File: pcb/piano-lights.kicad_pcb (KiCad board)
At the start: 2 copper layers, 98 x 51.6 mm, 40 parts, among them J1 USB-C 6-Pin, J2 FTDI RS232, J3 LED Strip, J4 AVR-ISP-6, J5 MIDI IN, J6 MIDI THRU, J7 MIDI Coupler B, J8 MIDI Coupler A, SW1 Button, SW2 Reset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

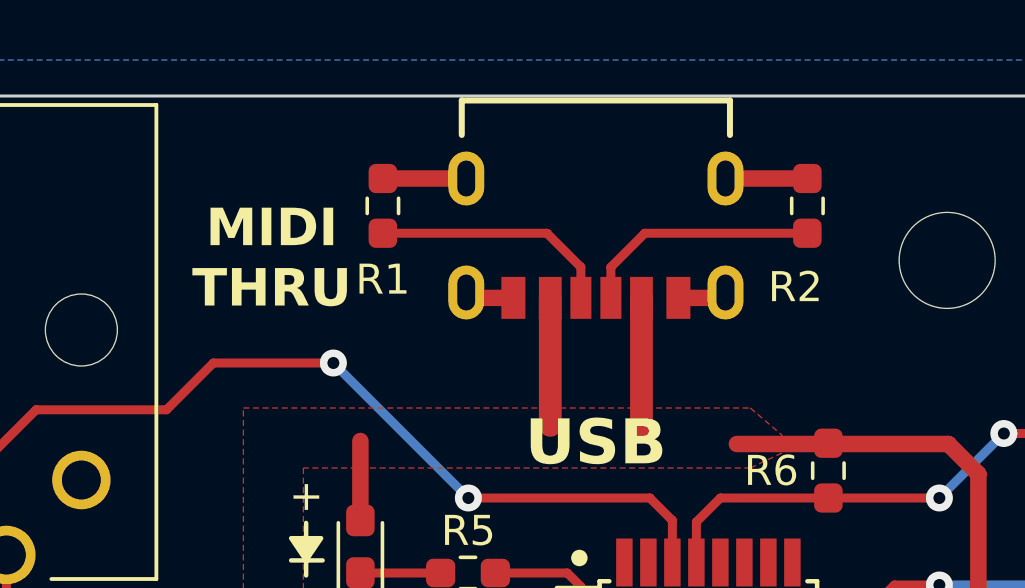
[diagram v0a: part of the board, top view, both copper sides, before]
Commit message: Tie USB-C shield to earth and add a 4n7F cap between earth and ground
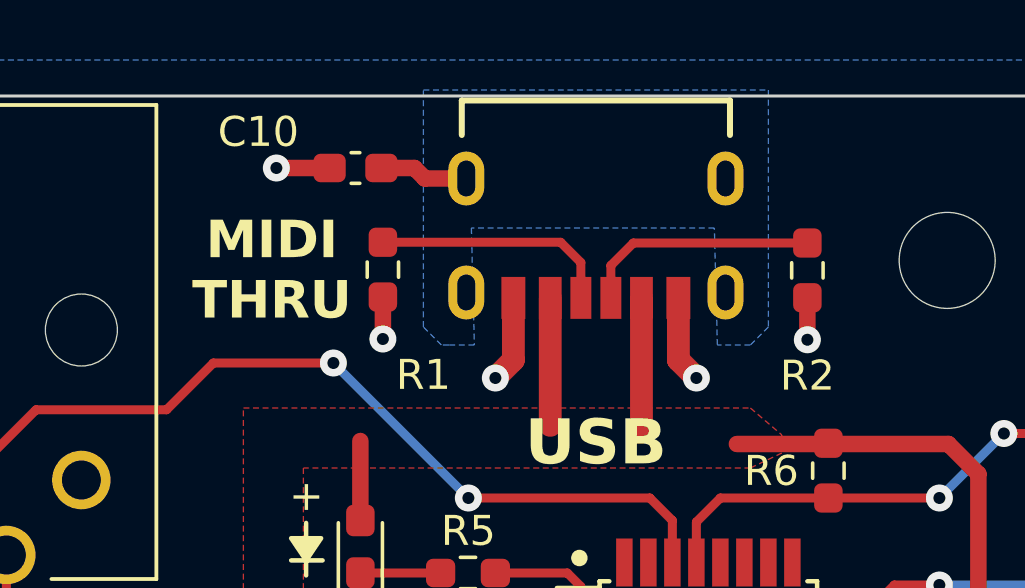
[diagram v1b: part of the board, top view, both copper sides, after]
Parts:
- added C10: 4n7, Capacitor_SMD:C_0603_1608Metric_Pad1.08x0.95mm_HandSolder, F.Cu at (149.8, 80.6)
- moved R2 2.15 mm to (164.9, 84.0), turned to -90 degrees
- moved R1 2.12 mm to (150.8, 84.0), turned to -90 degrees
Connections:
- J1 pad S1: GND -> Earth
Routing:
- net Earth: track 0.00 -> 2.97 mm
- net GND: track 32.7 -> 34.3 mm, vias 13 -> 18
- added copper zone on B.Cu, net Earth

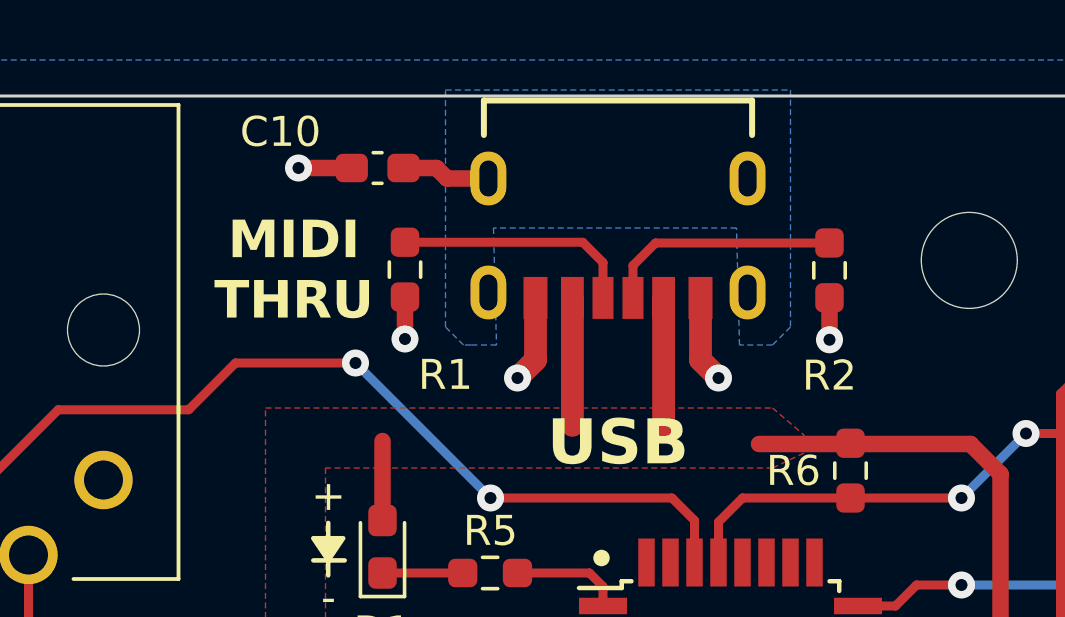
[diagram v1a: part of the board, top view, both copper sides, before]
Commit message: Reroute CC1 and CC2 to not cross ground split planes. Move Earth to front ground pour.
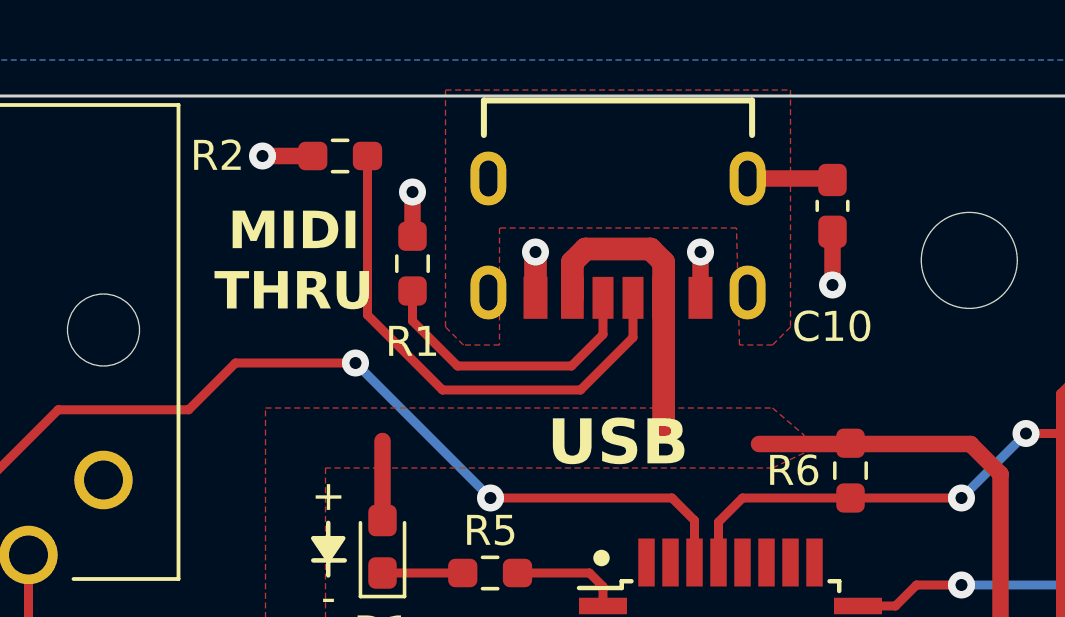
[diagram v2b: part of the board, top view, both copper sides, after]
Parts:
- moved R2 16.8 mm to (148.6, 80.2), turned to 180 degrees
- moved C10 15.2 mm to (165.0, 81.9), turned to 90 degrees
- moved R1 0.32 mm to (151.0, 83.8), turned to 90 degrees
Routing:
- net /USB_CC1: track 7.47 -> 17.2 mm
- net GND: track 34.3 -> 31.9 mm
- net /USB_CC2: track 7.71 -> 9.63 mm
- net +5V: track 130.0 -> 131.5 mm
- added copper zone on F.Cu, net Earth
- removed copper zone on B.Cu, net Earth

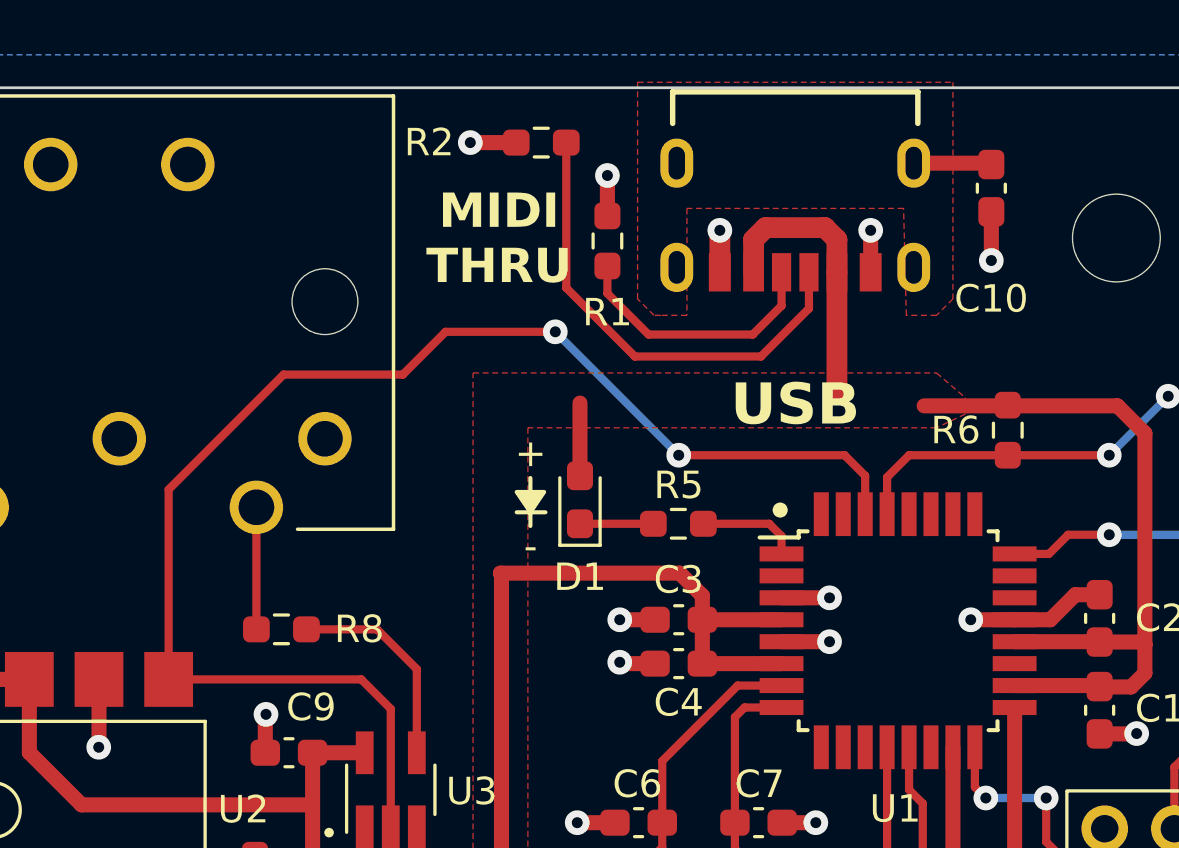
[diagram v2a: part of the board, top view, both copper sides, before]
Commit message: Rarrange CC1 and CC2 resistors to be next to each other
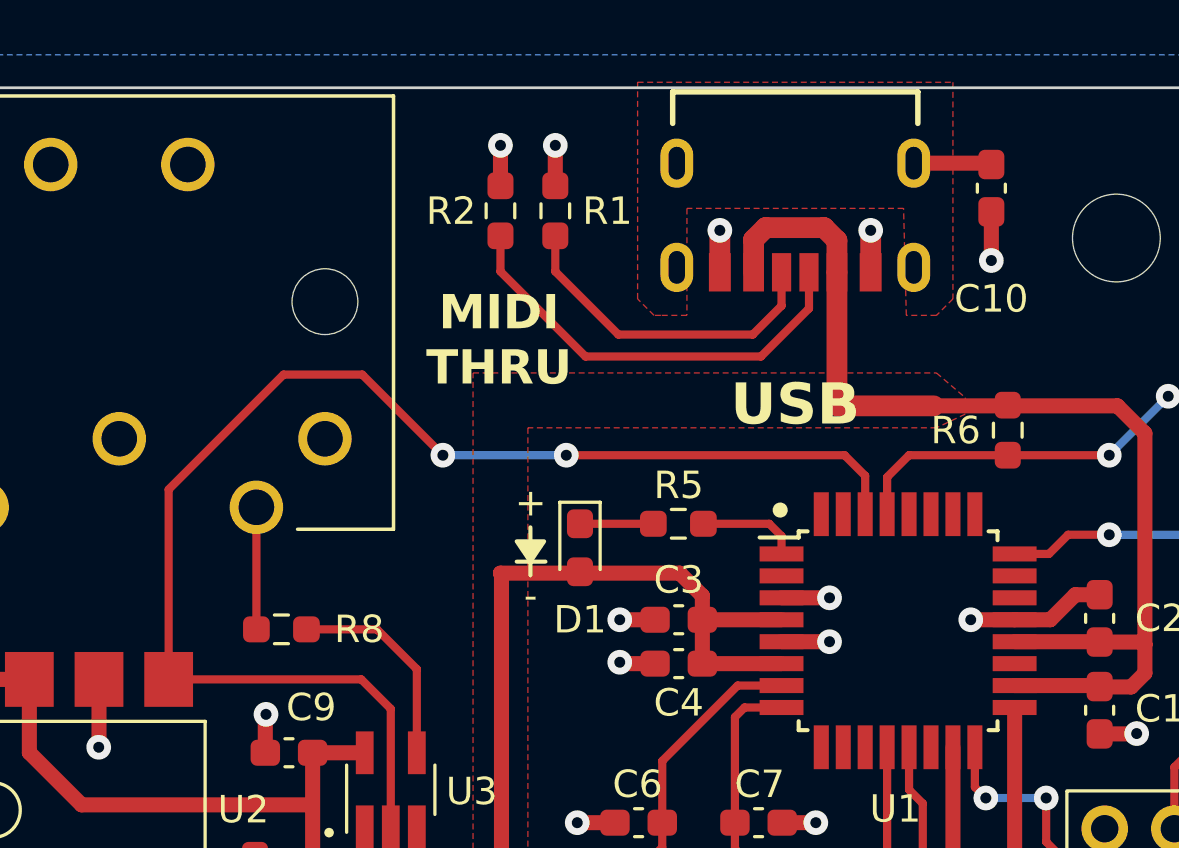
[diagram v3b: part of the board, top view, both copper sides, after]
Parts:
- moved R2 2.90 mm to (147.1, 82.7), turned to 90 degrees
- moved R1 2.20 mm to (149.1, 82.7)
- moved D1 1.75 mm to (150.0, 95.0), turned to -90 degrees
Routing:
- net /USB_CC2: track 9.63 -> 12.2 mm
- net +5V: track 131.5 -> 133.0 mm
- net /USB_CC1: track 17.2 -> 15.9 mm
- net /MIDI_RX: track 54.1 -> 52.8 mm

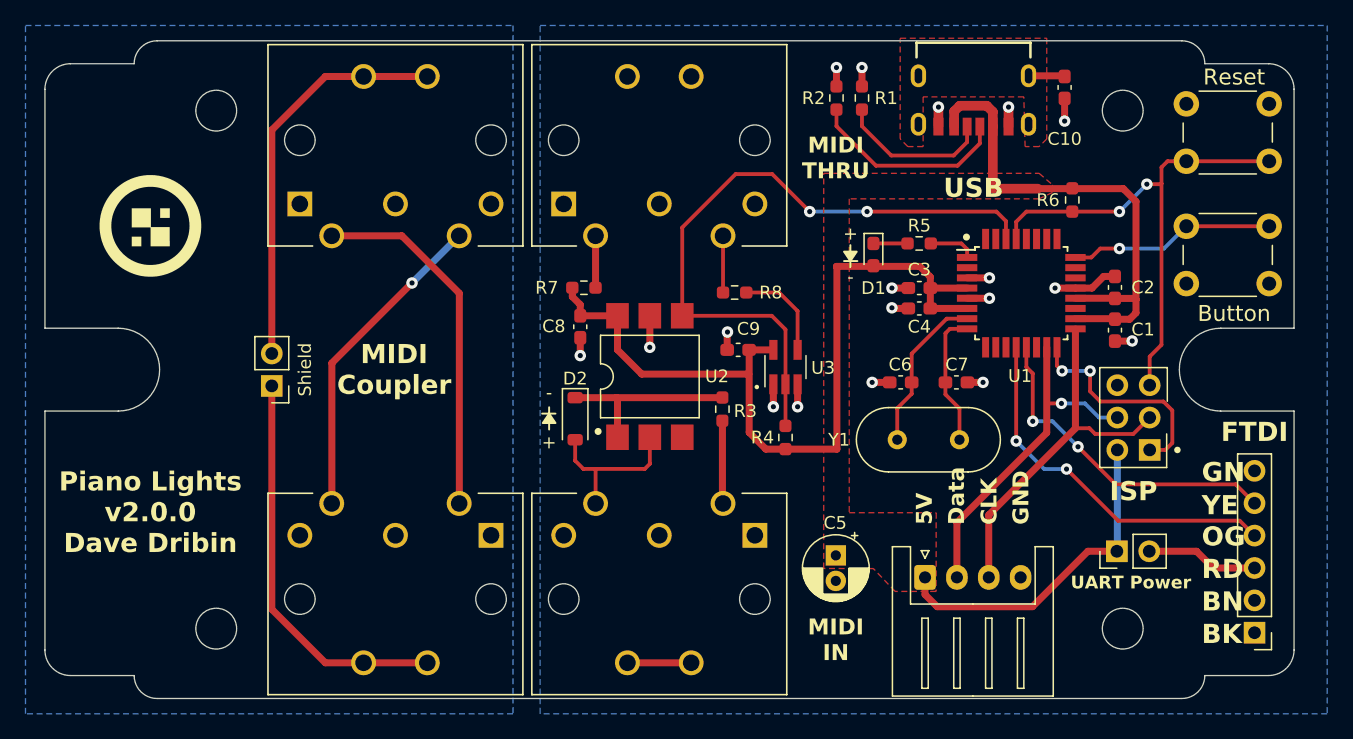
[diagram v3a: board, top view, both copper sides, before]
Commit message: Silkscreen tweaks
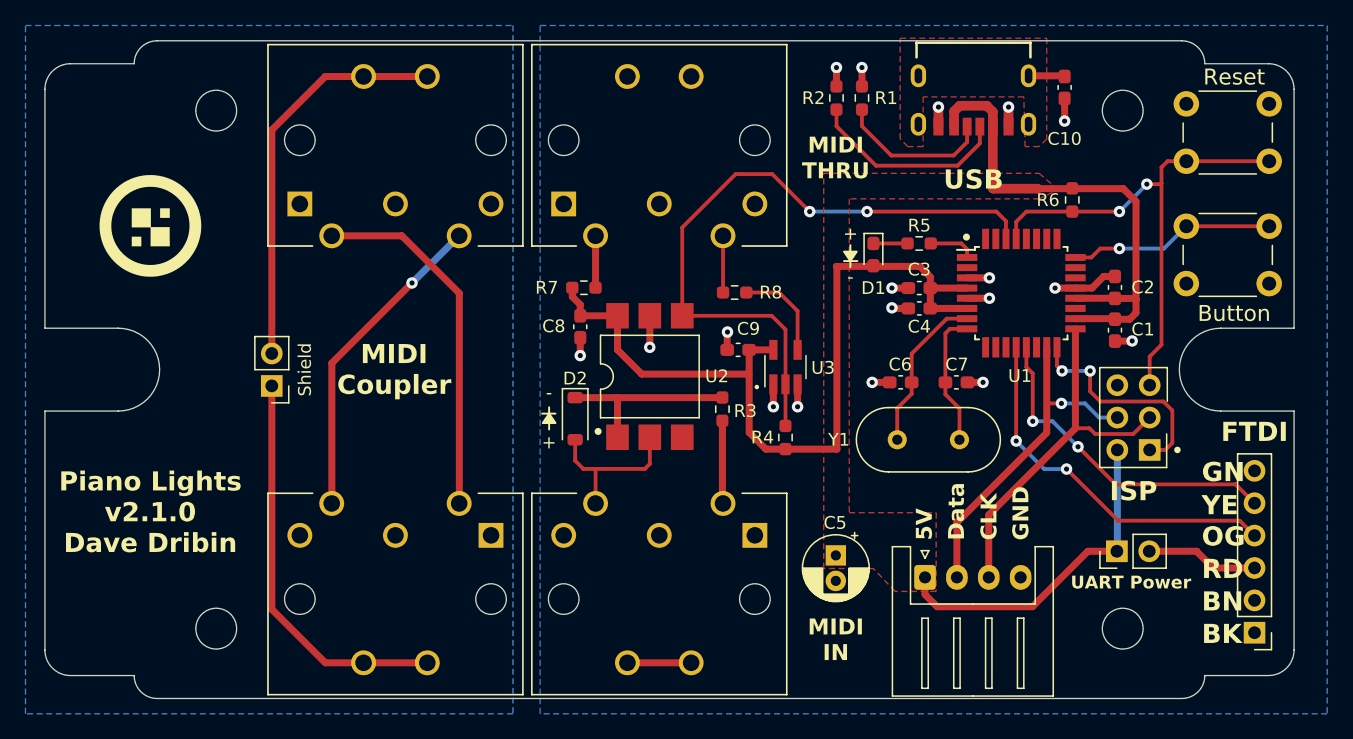
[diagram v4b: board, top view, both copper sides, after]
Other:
- board text added: "Piano Lights v2.1.0 Dave Dribin"
- board text removed: "Piano Lights v2.0.0 Dave Dribin"

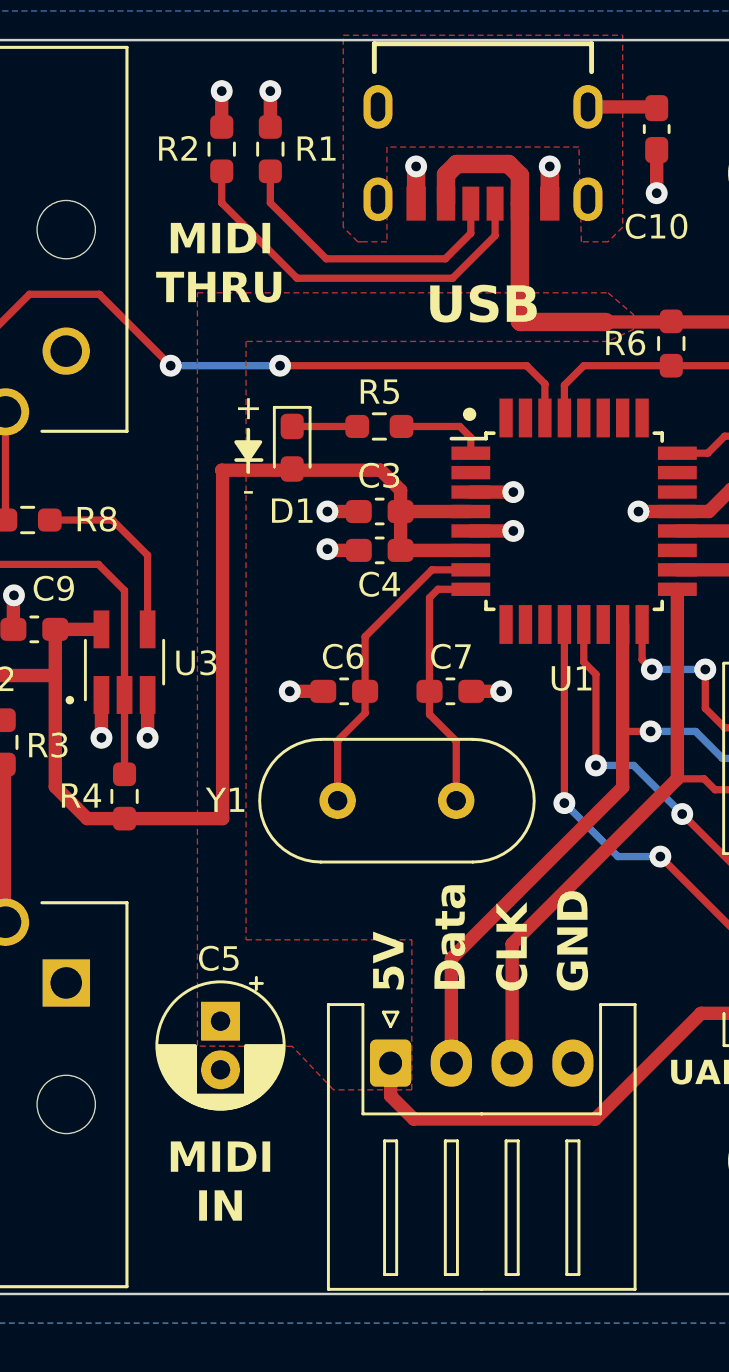
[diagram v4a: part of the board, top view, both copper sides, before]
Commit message: Move C5 down a bit, so it aligns with the connector
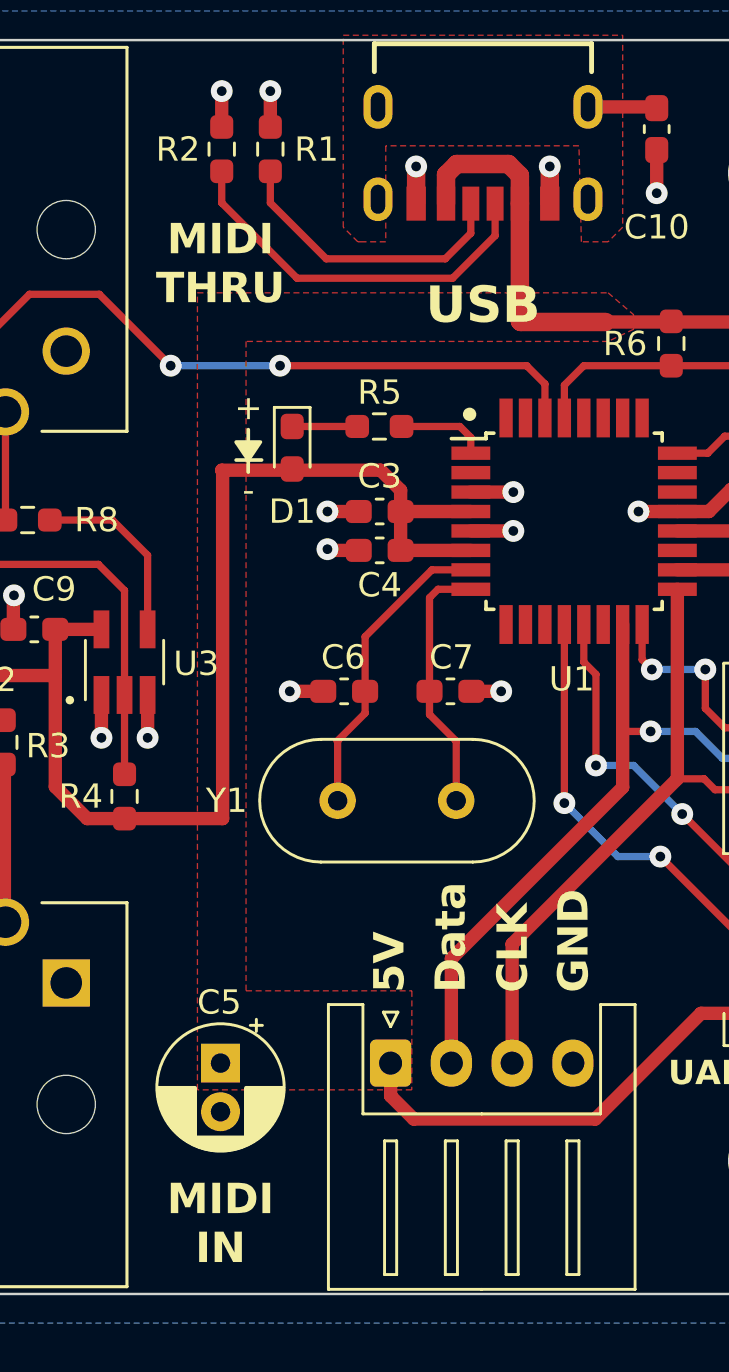
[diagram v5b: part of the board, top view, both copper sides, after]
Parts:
- moved C5 1.72 mm to (147.1, 120.3)
